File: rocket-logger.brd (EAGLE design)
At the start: 17 x 47.8 mm, 57 parts, among them IC1 CC430F513X, U1 MAX1555, X1 0896BM15A0001, X2 USB-MICROB, X3 SMA-142-0701-801/806

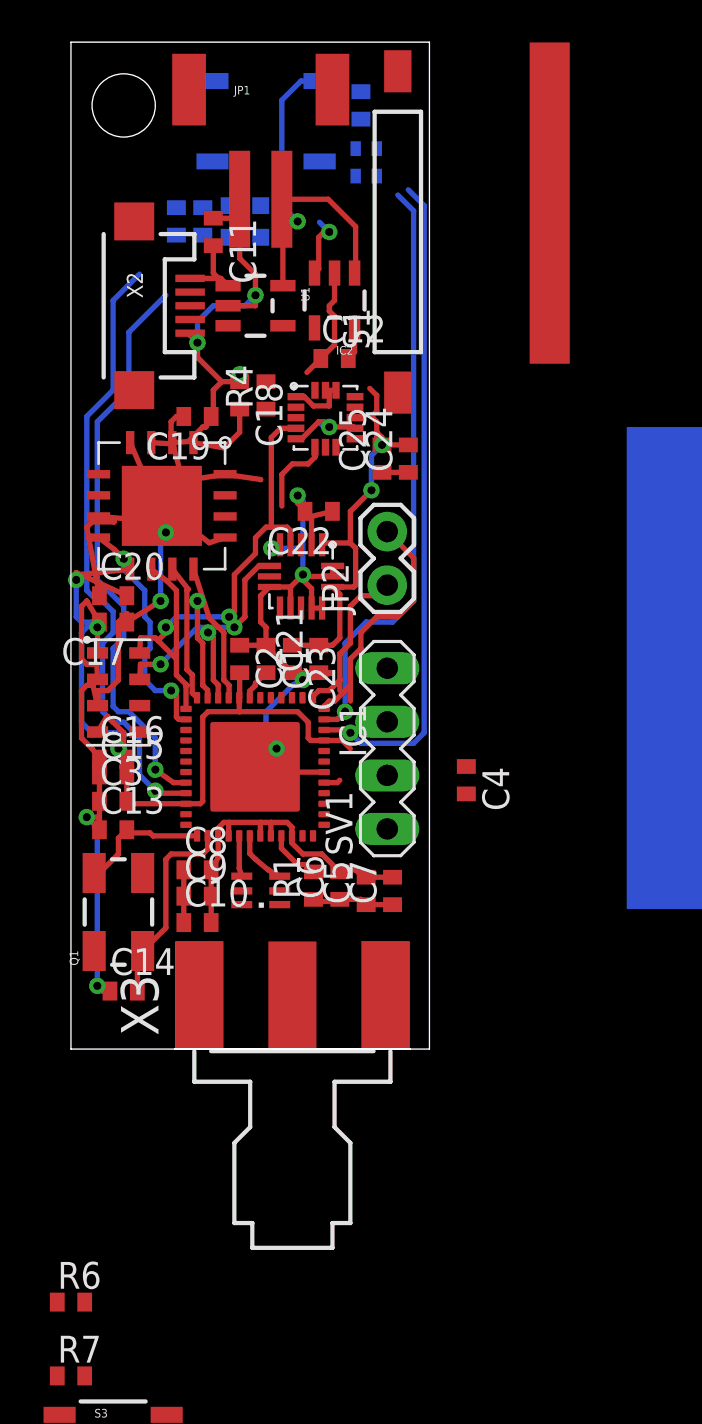
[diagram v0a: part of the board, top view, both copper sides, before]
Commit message: now with added flash
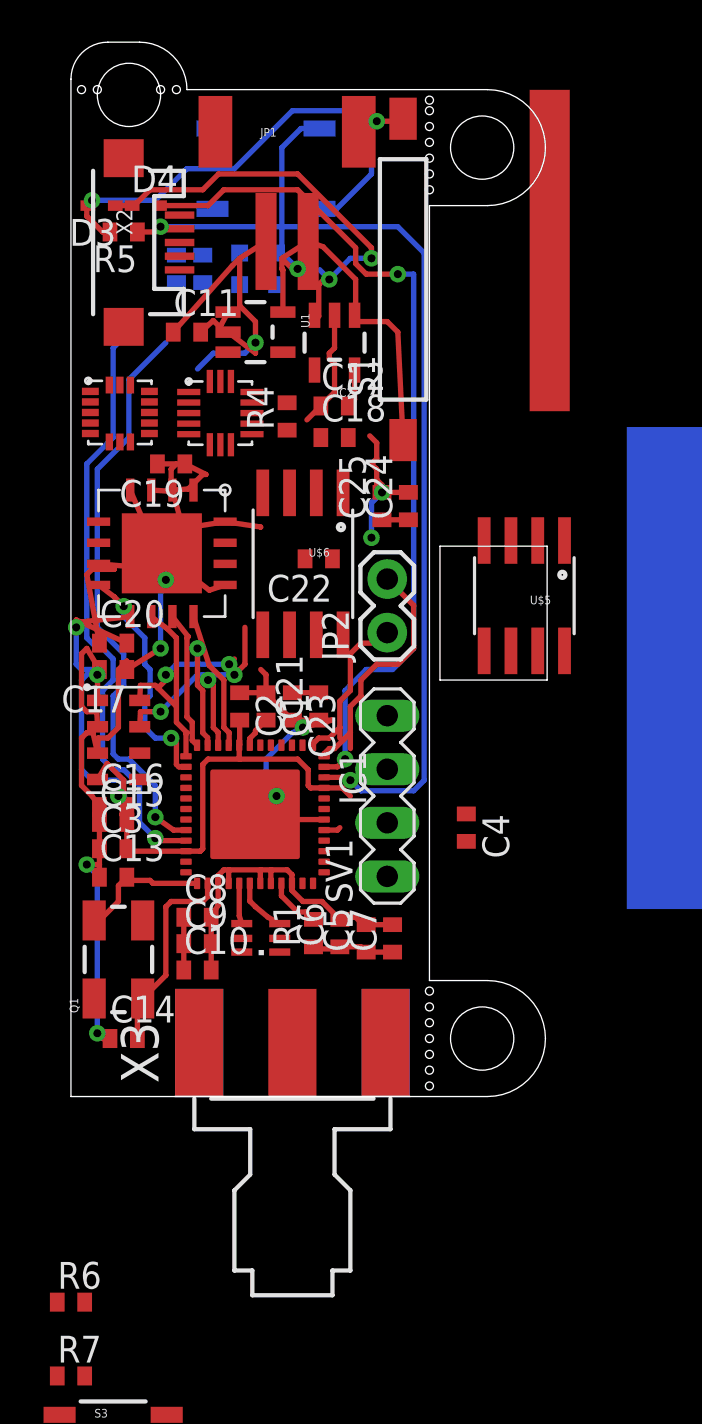
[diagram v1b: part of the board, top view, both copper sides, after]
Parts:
- added U$5: SPI_FLASH-X25XXSMD, SparkFun:SO08
- added U$6: SPI_FLASH-X25XXSMD1, SparkFun:SO08-EIAJ
- moved R5 12.8 mm to (2.50, 41.0), flipped to the top, turned to 180 degrees
- moved D3 12.2 mm to (1.50, 42.2), flipped to the top, turned to 180 degrees
- moved D4 11.2 mm to (3.50, 42.2), flipped to the top, turned to 0 degrees
- moved U$1 9.75 mm to (2.32, 32.4)
- moved U$3 8.64 mm to (7.08, 32.4), turned to 0 degrees
- moved C18 4.92 mm to (12.5, 31.2), turned to 0 degrees
- moved C11 4.91 mm to (5.50, 36.2), turned to 0 degrees
- moved X2 3.04 mm to (2.50, 40.5)
- moved C19 2.57 mm to (4.75, 30.0)
- moved LED2 2.37 mm to (9.75, 39.2), turned to 180 degrees
- moved JP1 2.36 mm to (10.2, 44.2)
- moved LED1 2.30 mm to (8.00, 39.2), turned to 180 degrees
- moved S1 2.26 mm to (15.8, 38.8)
- moved C1 2.25 mm to (9.25, 18.5)
- moved C10 2.25 mm to (6.00, 6.00)
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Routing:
- net N$24: track 0.00 -> 24.7 mm, vias 0 -> 2
- net GND: track 125.6 -> 104.3 mm, vias 13 -> 7
- net N$25: track 3.04 -> 20.1 mm, vias 1 -> 2
- net +3V3: track 67.4 -> 53.4 mm
- net SWITCHON: track 31.3 -> 44.4 mm, vias 1 -> 2
- net KEEPON: track 28.0 -> 40.7 mm, vias 1 -> 2
- net SCL: track 24.8 -> 12.7 mm
- net N$2: track 19.6 -> 25.9 mm
- net SDA: track 17.2 -> 11.9 mm
- net N$14: track 3.62 -> 0.00 mm
- net N$19: track 2.36 -> 0.00 mm
- net N$1: track 3.60 -> 2.01 mm
- net N$15: track 2.70 -> 3.25 mm
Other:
- board size 17 x 47.8 mm -> 22.6 x 50 mm
- board text added: "ACT"
- board text added: "ON"

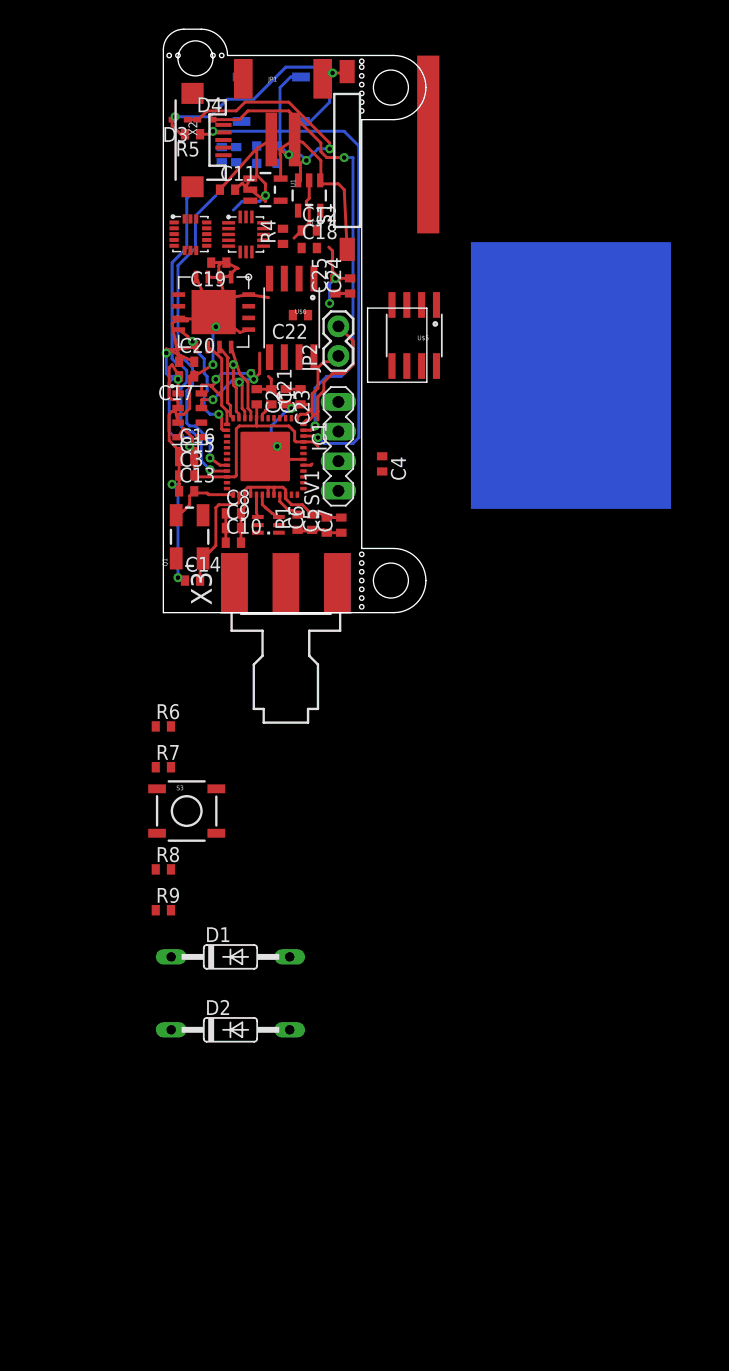
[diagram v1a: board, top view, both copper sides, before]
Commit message: added sounder layout
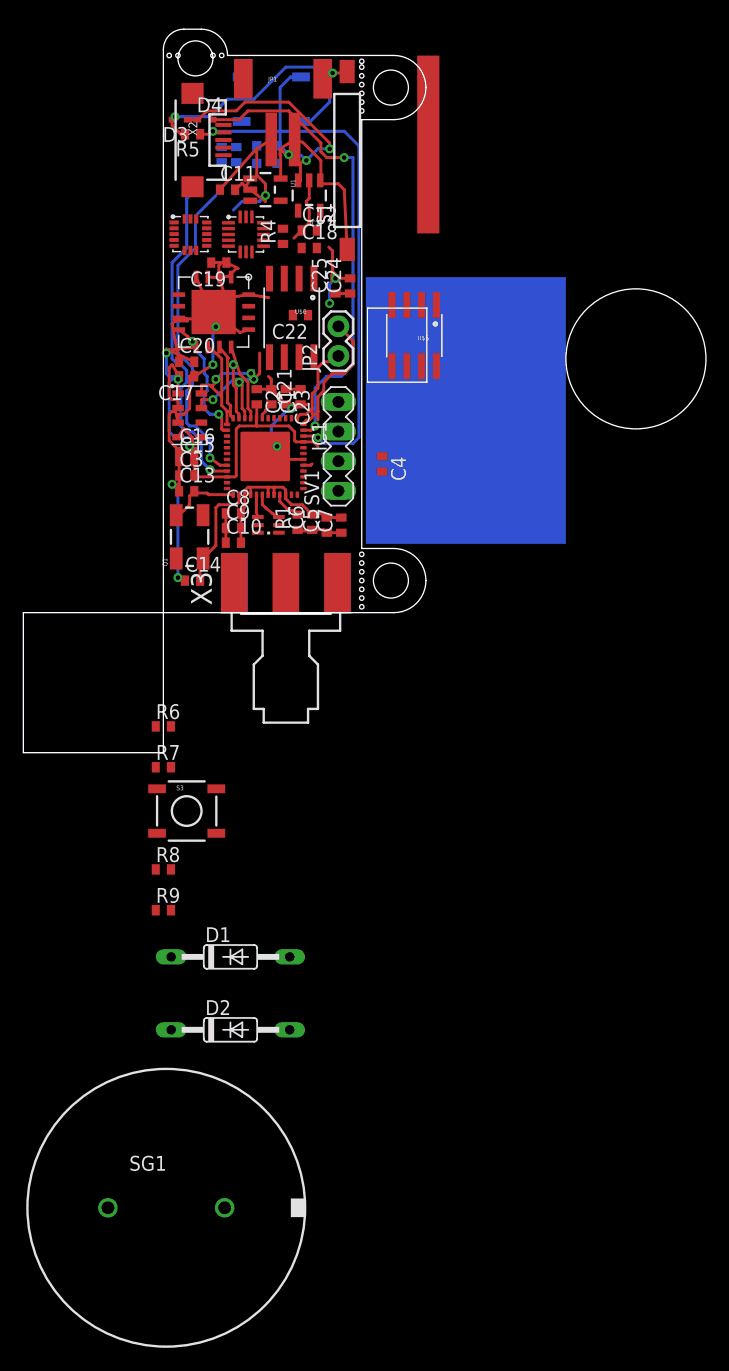
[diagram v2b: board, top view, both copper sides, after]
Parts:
- added SG1: EFBRD24C411, buzzer:EFBRD24C411
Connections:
- new net DSYNC: U$1.12
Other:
- board size 22.6 x 50 mm -> 58.5 x 62 mm
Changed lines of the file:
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@@
 <hole x="2.75" y="47.5" drill="3"/>
 <rectangle x1="21.75" y1="32.5" x2="23.655" y2="47.74" layer="1" rot="R180"/>
-<rectangle x1="26.355" y1="8.89" x2="43.5" y2="31.75" layer="16"/>
+<rectangle x1="17.355" y1="5.89" x2="34.5" y2="28.75" layer="16"/>
 <text x="10.25" y="37.75" size="1.016" layer="122" ratio="12" rot="MR270">ON</text>
 <text x="8.5" y="37.75" size="1.016" layer="122" ratio="12" rot="MR270">ACT</text>
@@
 <hole x="0.5" y="47.75" drill="0.381"/>
 <rectangle x1="17.5" y1="19.75" x2="22.58" y2="26.1" layer="20" rot="R180"/>
+<rectangle x1="-12" y1="-12" x2="0" y2="0" layer="20"/>
+<circle x="40.5" y="21.75" radius="6" width="0" layer="20"/>
 </plain>
 <attributes>
@@
 <element name="U$5" library="SparkFun" package="SO08" value="SPI_FLASH-X25XXSMD" x="21.5" y="23.75" rot="R180"/>
 <element name="U$6" library="SparkFun" package="SO08-EIAJ" value="SPI_FLASH-X25XXSMD1" x="11" y="25.25" rot="R180"/>
+<element name="SG1" library="buzzer" package="EFBRD24C411" value="EFBRD24C411" x="0.25" y="-51">
+<attribute name="OC_NEWARK" value="unknown" x="0.25" y="-51" size="1.016" layer="27" ratio="12" display="off"/>
+<attribute name="MPN" value="" x="0.25" y="-51" size="1.016" layer="27" ratio="12" display="off"/>
+<attribute name="MF" value="" x="0.25" y="-51" size="1.016" layer="27" ratio="12" display="off"/>
+<attribute name="OC_FARNELL" value="unknown" x="0.25" y="-51" size="1.016" layer="27" ratio="12" display="off"/>
+</element>
 </elements>
 <signals>
@@
 <wire x1="4.25" y1="41.25" x2="15.5" y2="41.25" width="0.254" layer="16"/>
 </signal>
+<signal name="DSYNC">
+<contactref element="U$1" pad="12"/>
+</signal>
 </signals>

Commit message: moving stuff around a bit
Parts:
- added S4: SWITCH-MOMENTARY-2SMD, SparkFun:TACTILE_SWITCH_SMD
- moved C23 14.5 mm to (19.2, 30.0), turned to 0 degrees
- moved C22 12.2 mm to (5.50, 36.0), turned to 0 degrees
- moved C11 4.65 mm to (8.25, 40.0), turned to 180 degrees
- moved S2 4.42 mm to (6.00, 41.0), turned to 270 degrees
- moved R4 2.85 mm to (12.5, 34.0)
- moved JP1 2.25 mm to (10.2, 46.5)
- moved IC2 2.02 mm to (12.8, 37.8)
- moved C12 1.77 mm to (13.8, 34.0), turned to 90 degrees
- moved U1 1.58 mm to (9.25, 37.8)
- moved U$3 1.27 mm to (8.34, 32.7)
- moved C18 0.71 mm to (13.0, 31.8), turned to 180 degrees
- moved U$1 0.56 mm to (2.82, 32.7)
- moved C21 0.35 mm to (12.0, 18.8)
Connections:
- new net CS_F: IC1.3, U$6.1
- new net HOLD: IC1.4, U$6.7
- new net N$27: U$6.3
- net +3V3: now also U$6.8
- net CLK: now also U$6.6
- net GND: now also U$6.4
- net MISO: now also U$6.2
- net MOSI: now also U$6.5
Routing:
- net GND: track 104.3 -> 76.5 mm, vias 7 -> 6
- net CS_F: track 0.00 -> 13.3 mm
- net N$2: track 25.9 -> 16.2 mm
- net MISO: track 11.5 -> 19.0 mm
- net MOSI: track 6.58 -> 13.0 mm, vias 0 -> 2
- net HOLD: track 0.00 -> 5.92 mm
- net +3V3: track 53.4 -> 48.3 mm
- net N$15: track 3.25 -> 0.00 mm
- net N$24: track 24.7 -> 21.6 mm
- net N$1: track 2.01 -> 0.00 mm
- net CLK: track 7.41 -> 9.41 mm
- net N$25: track 20.1 -> 18.4 mm
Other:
- outline, holes or cut-outs redrawn
- board text added: "TOP"

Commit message: routing
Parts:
- added C26: (no value), resistor:C0402
- added L1: (no value), wuerth-elektronik:0603
- moved R7 48.3 mm to (11.5, 33.6), turned to 90 degrees
- moved R6 30.4 mm to (2.13, 20.6)
- moved R5 18.5 mm to (15.8, 28.2), turned to 90 degrees
- moved D3 16.1 mm to (13.5, 31.5), turned to 0 degrees
- moved D4 15.4 mm to (13.5, 30.5)
- moved C23 15.4 mm to (5.23, 36.3)
- moved C18 5.92 mm to (7.31, 30.1)
- moved C24 5.62 mm to (20.3, 31.7)
- moved LED2 5.38 mm to (5.66, 35.8), turned to 90 degrees
- moved R2 4.04 mm to (2.88, 37.0), turned to 180 degrees
- moved C16 4.03 mm to (0.00, 10.2), turned to 90 degrees
- moved R3 4.01 mm to (2.88, 35.8), turned to 180 degrees
- moved LED1 3.21 mm to (5.66, 37.1), turned to 90 degrees
- moved C13 2.26 mm to (2.25, 8.15)
- moved C15 2.26 mm to (2.25, 10.8)
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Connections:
- new net N$23: IC1.39, SV1.4
- new net N$26: IC1.40, SV1.3
- new net N$28: IC1.2, S4.3
- net +3V3: now also L1.2
- net AVCC_RF2: now also L1.1
- net GND: now also C26.1, LED1.C, LED2.C; no longer R2.2, R3.2
- net N$10: now also LED2.A, R3.2; no longer LED2.C, R3.1
- net N$16: now also R2.1; no longer LED1.A
- net N$17: now also R3.1; no longer LED2.A
- net N$2: now also C26.2
- net N$9: now also LED1.A, R2.2; no longer LED1.C, R2.1
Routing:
- net +3V3: track 48.3 -> 93.0 mm, vias 5 -> 4
- net N$28: track 0.00 -> 36.7 mm, vias 0 -> 1
- net GND: track 76.5 -> 110.7 mm, vias 6 -> 11
- net SWITCHON: track 44.4 -> 18.0 mm, vias 2 -> 0
- net SDA: track 11.9 -> 38.1 mm
- net SCL: track 12.7 -> 34.7 mm, vias 3 -> 4
- net KEEPON: track 40.7 -> 19.1 mm
- net CLK: track 9.41 -> 17.9 mm, vias 0 -> 2
- net N$25: track 18.4 -> 11.8 mm, vias 2 -> 0
- net HOLD: track 5.92 -> 11.7 mm
- net N$1: track 0.00 -> 5.63 mm
- net N$24: track 21.6 -> 26.5 mm, vias 2 -> 1
- net MISO: track 19.0 -> 23.9 mm, vias 2 -> 3
- net N$2: track 16.2 -> 19.6 mm
- net N$23: track 0.00 -> 3.38 mm
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
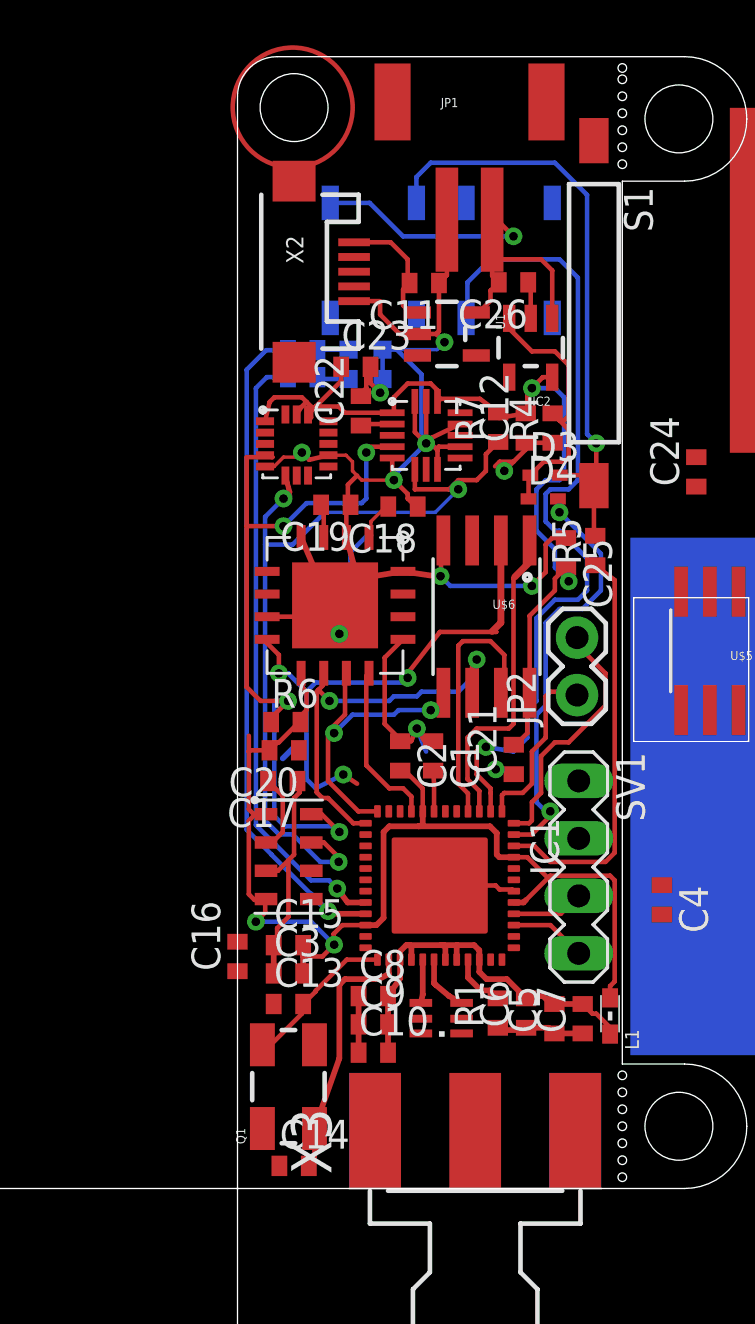
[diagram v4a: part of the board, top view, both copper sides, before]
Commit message: wired sounder
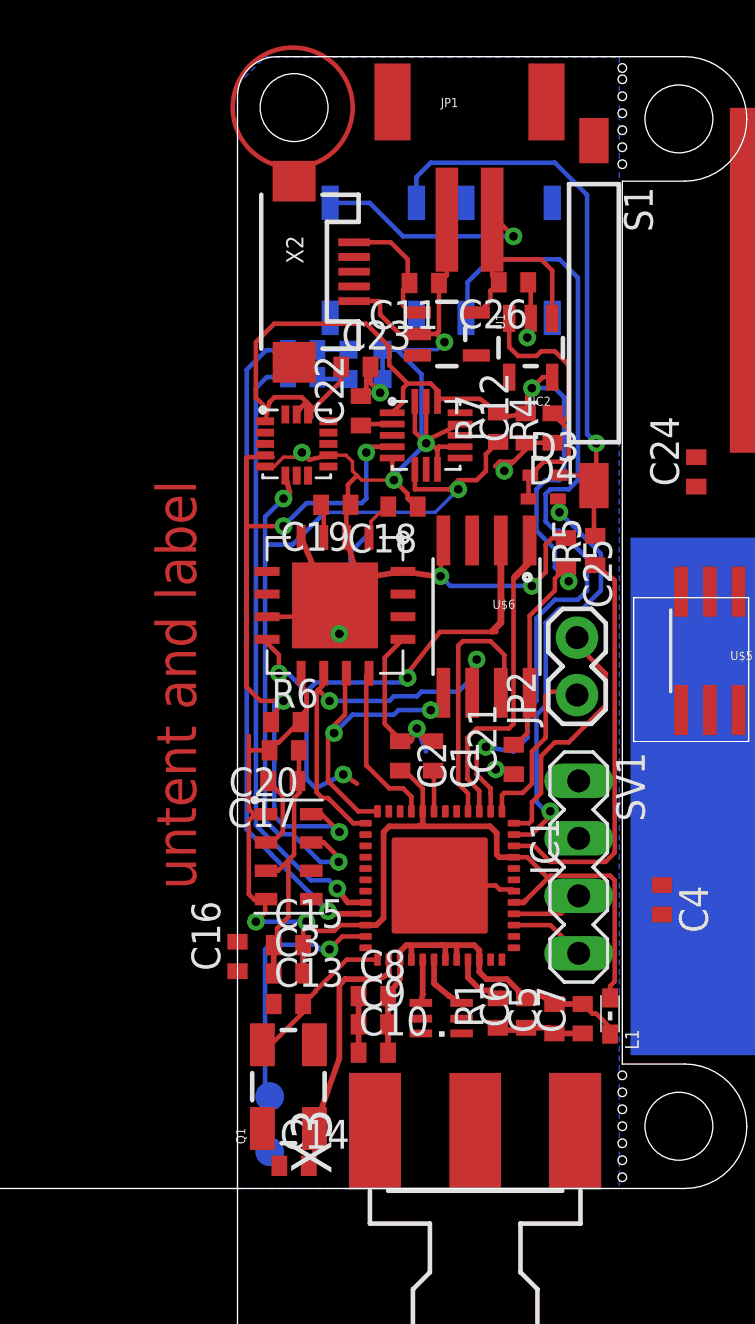
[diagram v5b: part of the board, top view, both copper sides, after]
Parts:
- added TP1, TP2: PTR1B1,27, testpad:B1,27
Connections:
- new net N$29: IC1.23, TP1.TP
- net GND: now also TP2.TP
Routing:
- net N$29: track 0.00 -> 11.4 mm, vias 0 -> 1
- net +3V3: track 93.0 -> 100.2 mm
- net GND: track 110.7 -> 113.1 mm, vias 11 -> 12
- net N$17: track 27.9 -> 27.2 mm
- net N$25: track 11.8 -> 12.5 mm
- net SCL: track 34.7 -> 34.2 mm
- added copper zone on layer 16, net GND
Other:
- board text added: "untent and label"
